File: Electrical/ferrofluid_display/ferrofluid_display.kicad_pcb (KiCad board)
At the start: 2 copper layers, 627 parts, among them J1001 Screw_Terminal_01x06, U100001 DRV8872DDAR, U10001 DRV8872DDAR, U1001 74HC595, U101001 DRV8872DDAR, U102001 DRV8872DDAR, U103001 DRV8872DDAR, U105001 DRV8872DDAR, U106001 DRV8872DDAR, U107001 DRV8872DDAR, U108001 DRV8872DDAR, U109001 DRV8872DDAR, U110001 DRV8872DDAR, U11001 DRV8872DDAR, U111001 DRV8872DDAR, U112001 DRV8872DDAR, U113001 DRV8872DDAR, U114001 DRV8872DDAR, U12001 DRV8872DDAR, U13001 DRV8872DDAR, U14001 DRV8872DDAR, U15001 DRV8872DDAR, U17001 DRV8872DDAR, U18001 DRV8872DDAR, U19001 DRV8872DDAR, U20001 DRV8872DDAR, U2002 74HC595, U2003 74HC595, U2004 74HC595, U2005 74HC595, U2006 74HC595, U2007 74HC595, U2008 74HC595, U2009 74HC595, U21001 DRV8872DDAR, U22001 DRV8872DDAR, U23001 DRV8872DDAR, U24001 DRV8872DDAR, U25001 DRV8872DDAR, U26001 DRV8872DDAR, U28001 DRV8872DDAR, U29001 DRV8872DDAR, U30001 DRV8872DDAR, U3002 74HC595, U3003 74HC595, U3004 74HC595, U3005 74HC595, U3006 74HC595, U3007 74HC595, U3008 74HC595, U3009 74HC595, U31001 DRV8872DDAR, U32001 DRV8872DDAR, U33001 DRV8872DDAR, U34001 DRV8872DDAR, U35001 DRV8872DDAR, U36001 DRV8872DDAR, U37001 DRV8872DDAR, U39001 DRV8872DDAR, U40001 DRV8872DDAR, U4002 74HC595, U4003 74HC595, U4004 74HC595, U4005 74HC595, U4006 74HC595, U4007 74HC595, U4008 74HC595, U4009 74HC595, U41001 DRV8872DDAR, U42001 DRV8872DDAR, U43001 DRV8872DDAR, U44001 DRV8872DDAR, U45001 DRV8872DDAR, U46001 DRV8872DDAR, U47001 DRV8872DDAR, U48001 DRV8872DDAR, U50001 DRV8872DDAR, U51001 DRV8872DDAR, U52001 DRV8872DDAR, U53001 DRV8872DDAR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

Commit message: Auto-layed out file
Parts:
- moved R26002 272.6 mm to (277.5, 0.03)
- moved U26001 272.5 mm to (279.5, 6.05)
- moved U112001 271.5 mm to (247.5, 118.0)
- moved L112001 271.1 mm to (253.2, 117.9), turned to 90 degrees
- moved R15002 270.9 mm to (277.5, -14.0)
- moved D26002 270.6 mm to (281.2, -0.10), turned to 180 degrees
- moved U103001 270.5 mm to (279.5, 104.0)
- moved L103001 270.0 mm to (285.2, 103.9), turned to 90 degrees
- moved U15001 268.9 mm to (279.5, -7.95)
- moved L26001 268.6 mm to (285.2, 5.87), turned to 90 degrees
- moved D15002 268.2 mm to (281.2, -14.1), turned to 180 degrees
- moved D112002 266.0 mm to (249.2, 111.9), turned to 180 degrees
- moved D103002 265.0 mm to (281.2, 97.9), turned to 180 degrees
- moved R112002 264.9 mm to (245.5, 112.0)
- moved R103002 264.1 mm to (277.5, 98.0)
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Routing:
- net GND: track 0.00 -> 340.6 mm, vias 0 -> 200
- net Net-(D68002-Pad1): track 0.00 -> 14.0 mm
- net Net-(D67002-Pad1): track 0.00 -> 14.0 mm
- net Net-(D66002-Pad1): track 0.00 -> 14.0 mm
- net Net-(D65002-Pad1): track 0.00 -> 14.0 mm
- net Net-(D64002-Pad1): track 0.00 -> 14.0 mm
- net Net-(D63002-Pad1): track 0.00 -> 14.0 mm
- net Net-(D62002-Pad1): track 0.00 -> 14.0 mm
- net Net-(D61002-Pad1): track 0.00 -> 14.0 mm
- net Net-(D57002-Pad1): track 0.00 -> 14.0 mm
- net Net-(D56002-Pad1): track 0.00 -> 14.0 mm
- net Net-(D55002-Pad1): track 0.00 -> 14.0 mm
- net Net-(D54002-Pad1): track 0.00 -> 14.0 mm
- net Net-(D53002-Pad1): track 0.00 -> 14.0 mm
- net Net-(D52002-Pad1): track 0.00 -> 14.0 mm
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
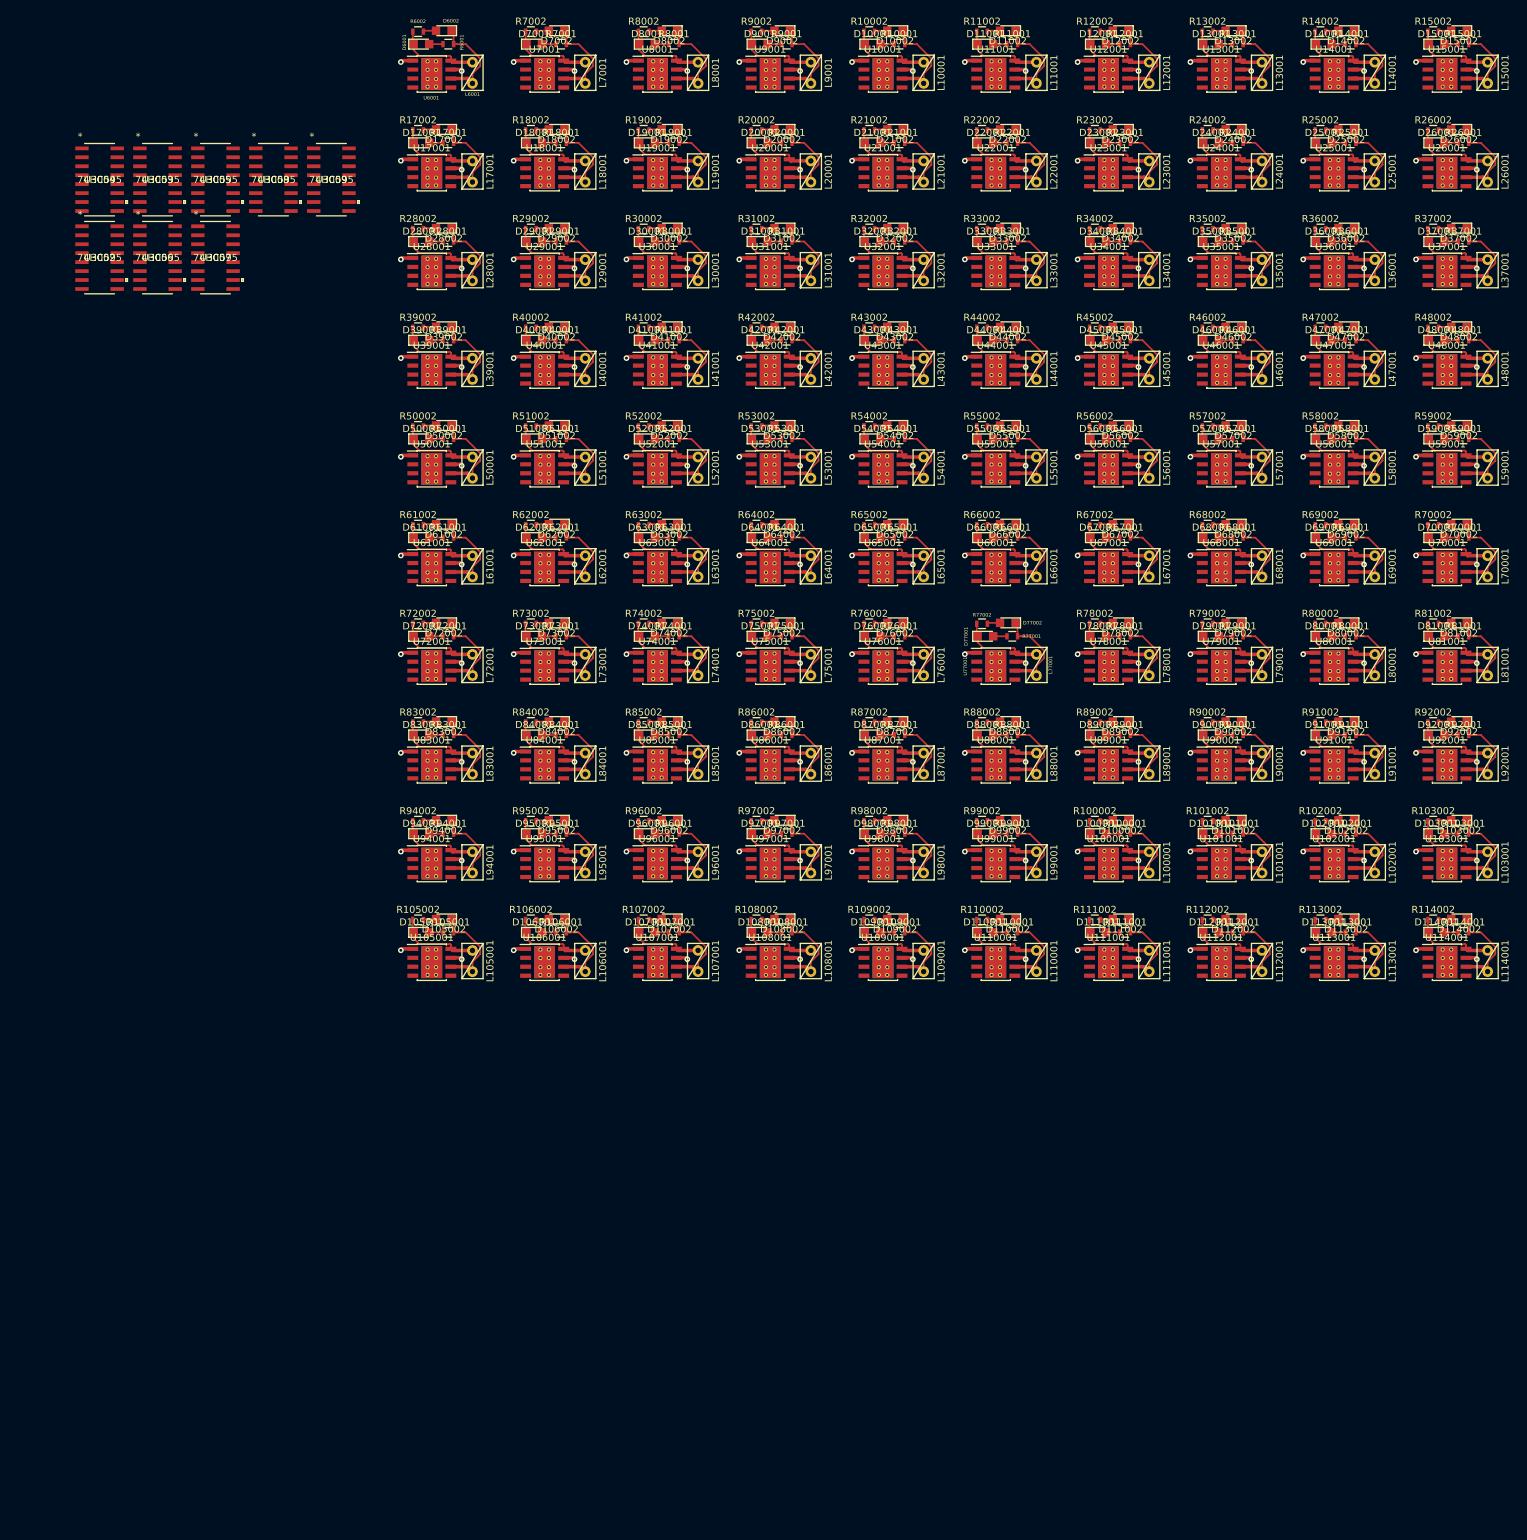
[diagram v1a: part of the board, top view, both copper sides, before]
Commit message: Added layers and 5V via
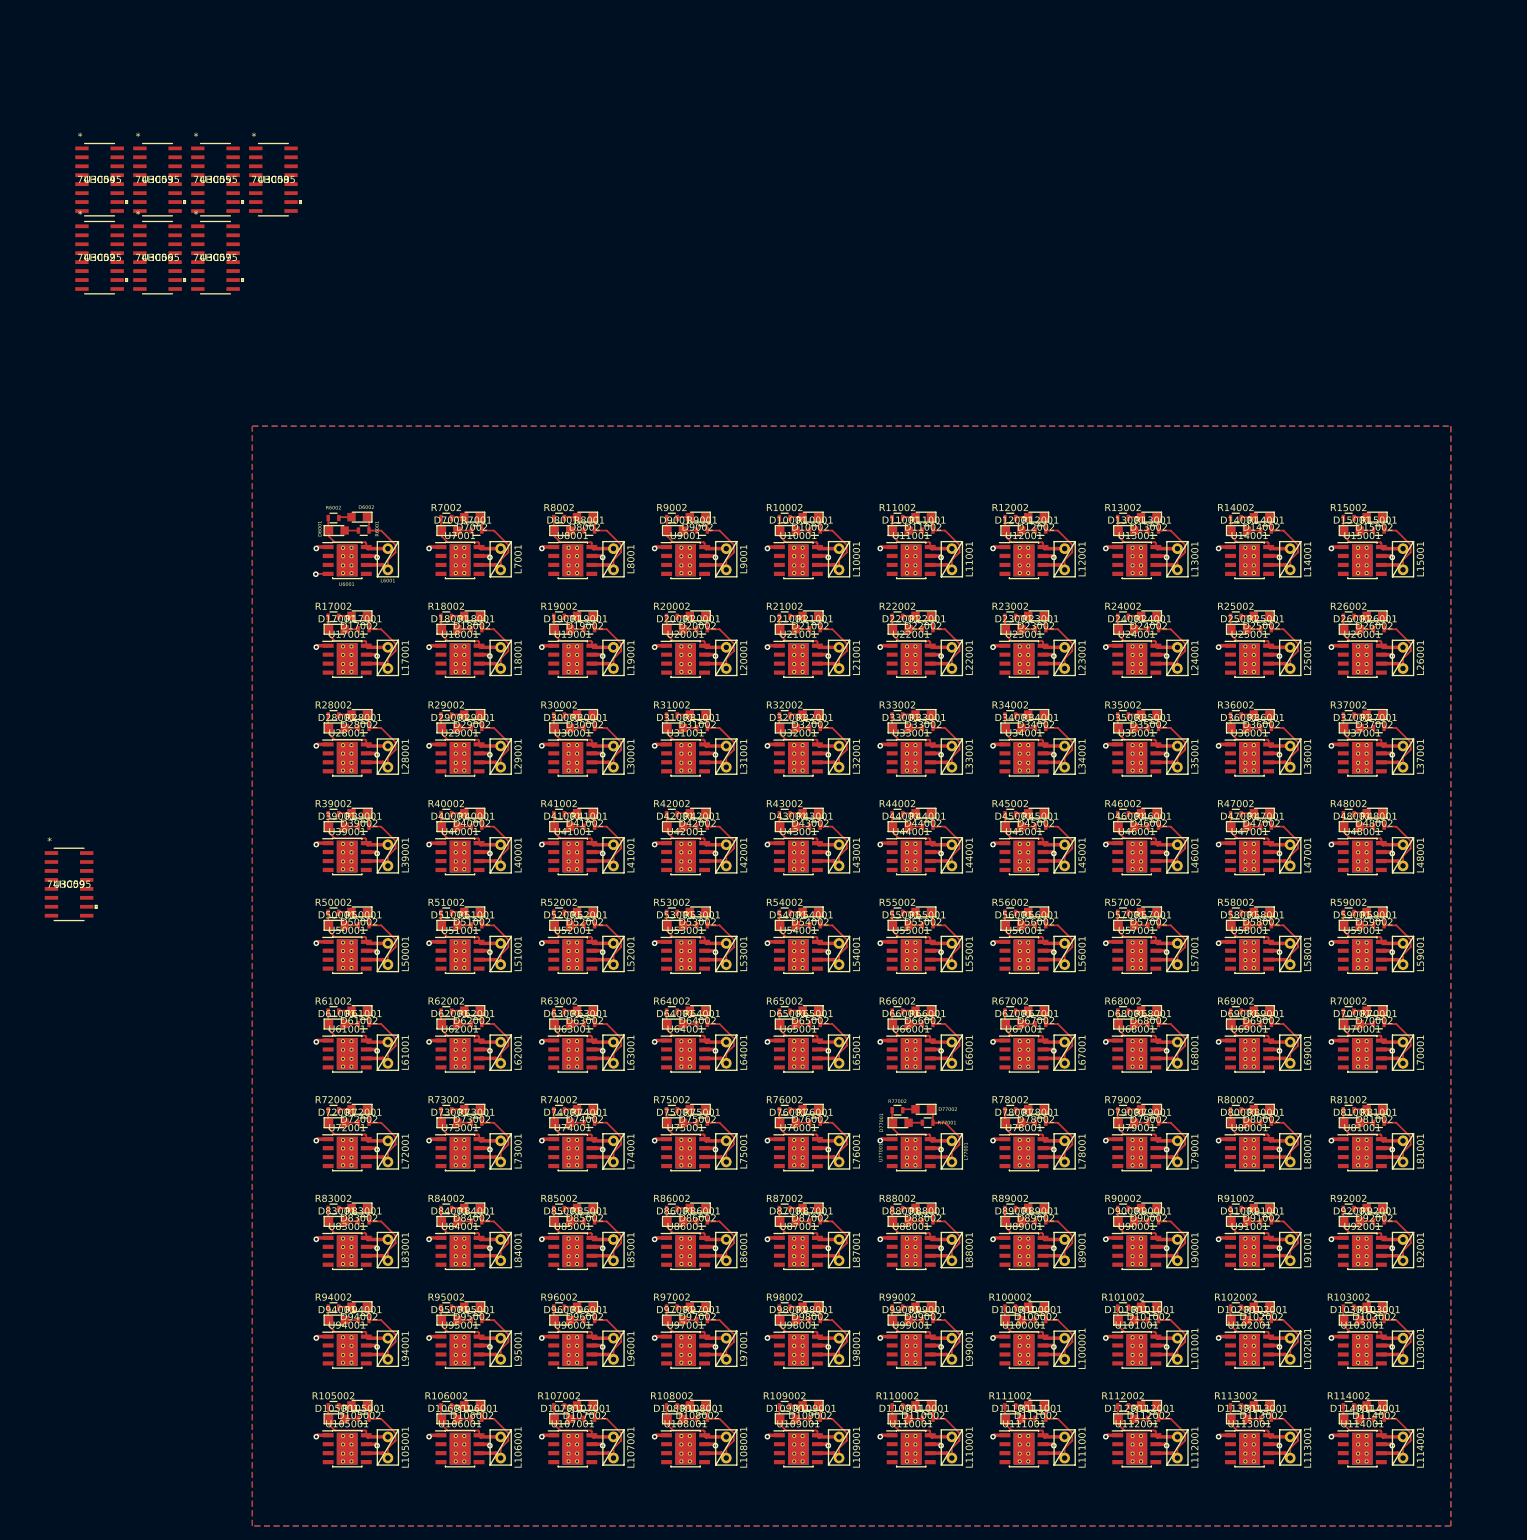
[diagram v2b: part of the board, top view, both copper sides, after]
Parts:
- moved U3009 106.7 mm to (84.0, 107.0)
- moved L100001 70.0 mm to (225.2, 172.9)
- moved L101001 70.0 mm to (241.2, 172.9)
- moved L102001 70.0 mm to (257.2, 172.9)
- moved L103001 70.0 mm to (273.2, 172.9)
- moved L105001 70.0 mm to (129.2, 186.9)
- moved L106001 70.0 mm to (145.2, 186.9)
- moved L107001 70.0 mm to (161.2, 186.9)
- moved L108001 70.0 mm to (177.2, 186.9)
- moved L109001 70.0 mm to (193.2, 186.9)
- moved L110001 70.0 mm to (209.2, 186.9)
- moved L111001 70.0 mm to (225.2, 186.9)
- moved L112001 70.0 mm to (241.2, 186.9)
- moved L113001 70.0 mm to (257.2, 186.9)
- moved L114001 70.0 mm to (273.2, 186.9)
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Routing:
- net +5V: track 0.00 -> 1.78 mm, vias 0 -> 1
- added copper zone on F.Cu, net +12V
- added copper zone on In1.Cu, net +5V
- added copper zone on B.Cu, net GND
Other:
- copper layers 2 -> 4

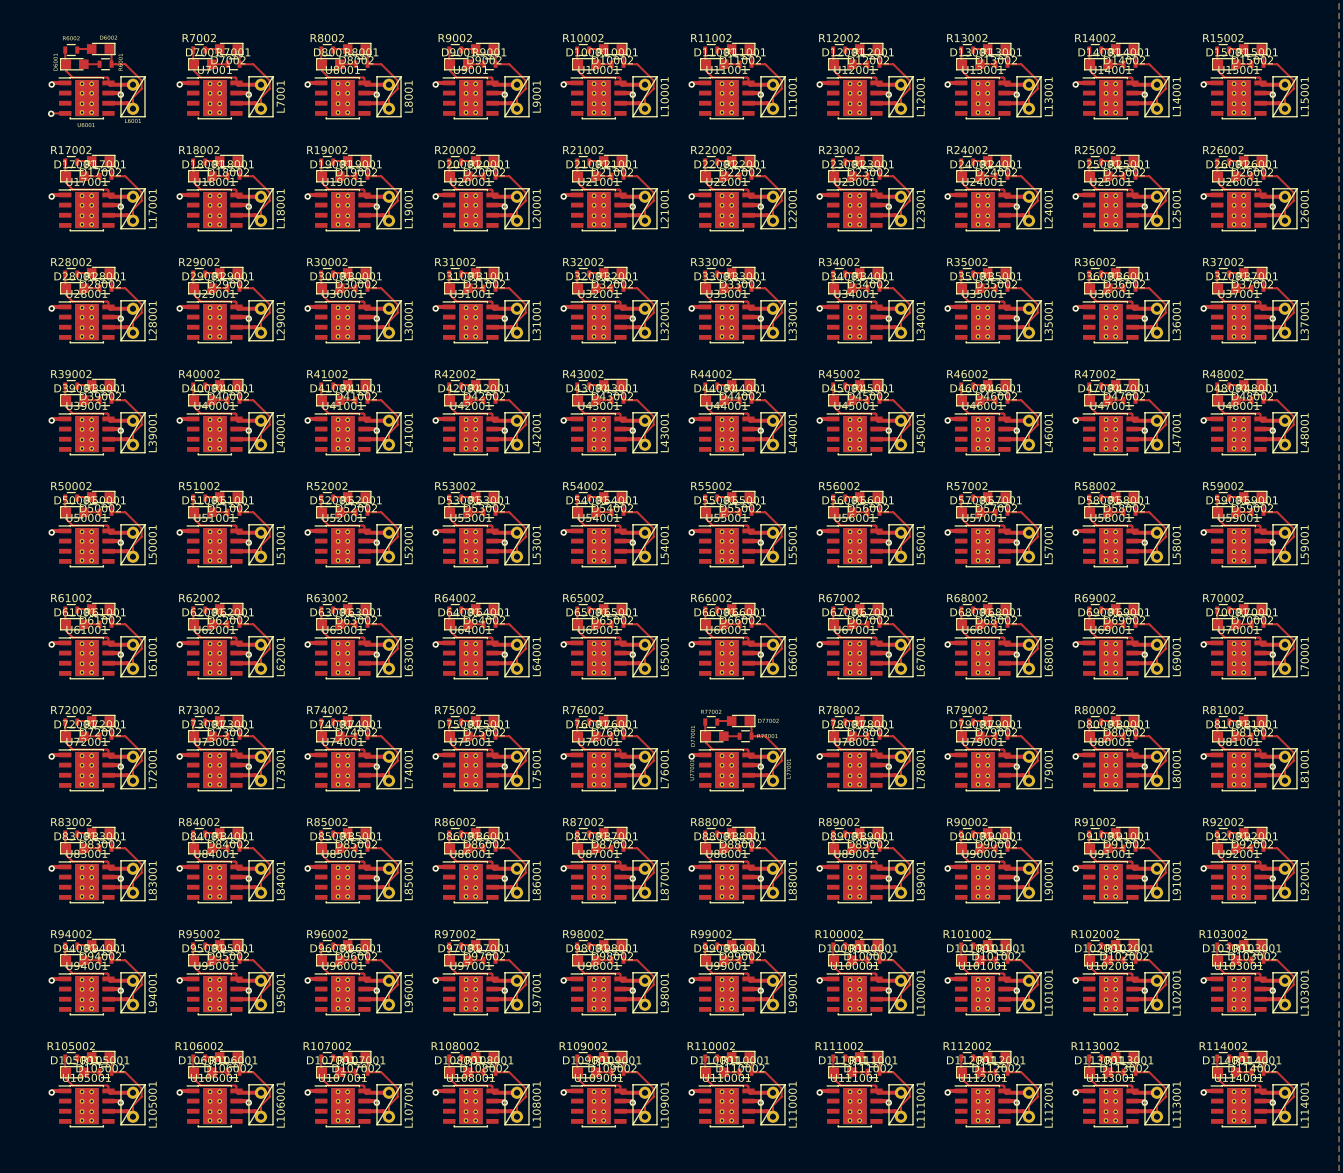
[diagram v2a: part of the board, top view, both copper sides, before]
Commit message: Propegated 5V changes
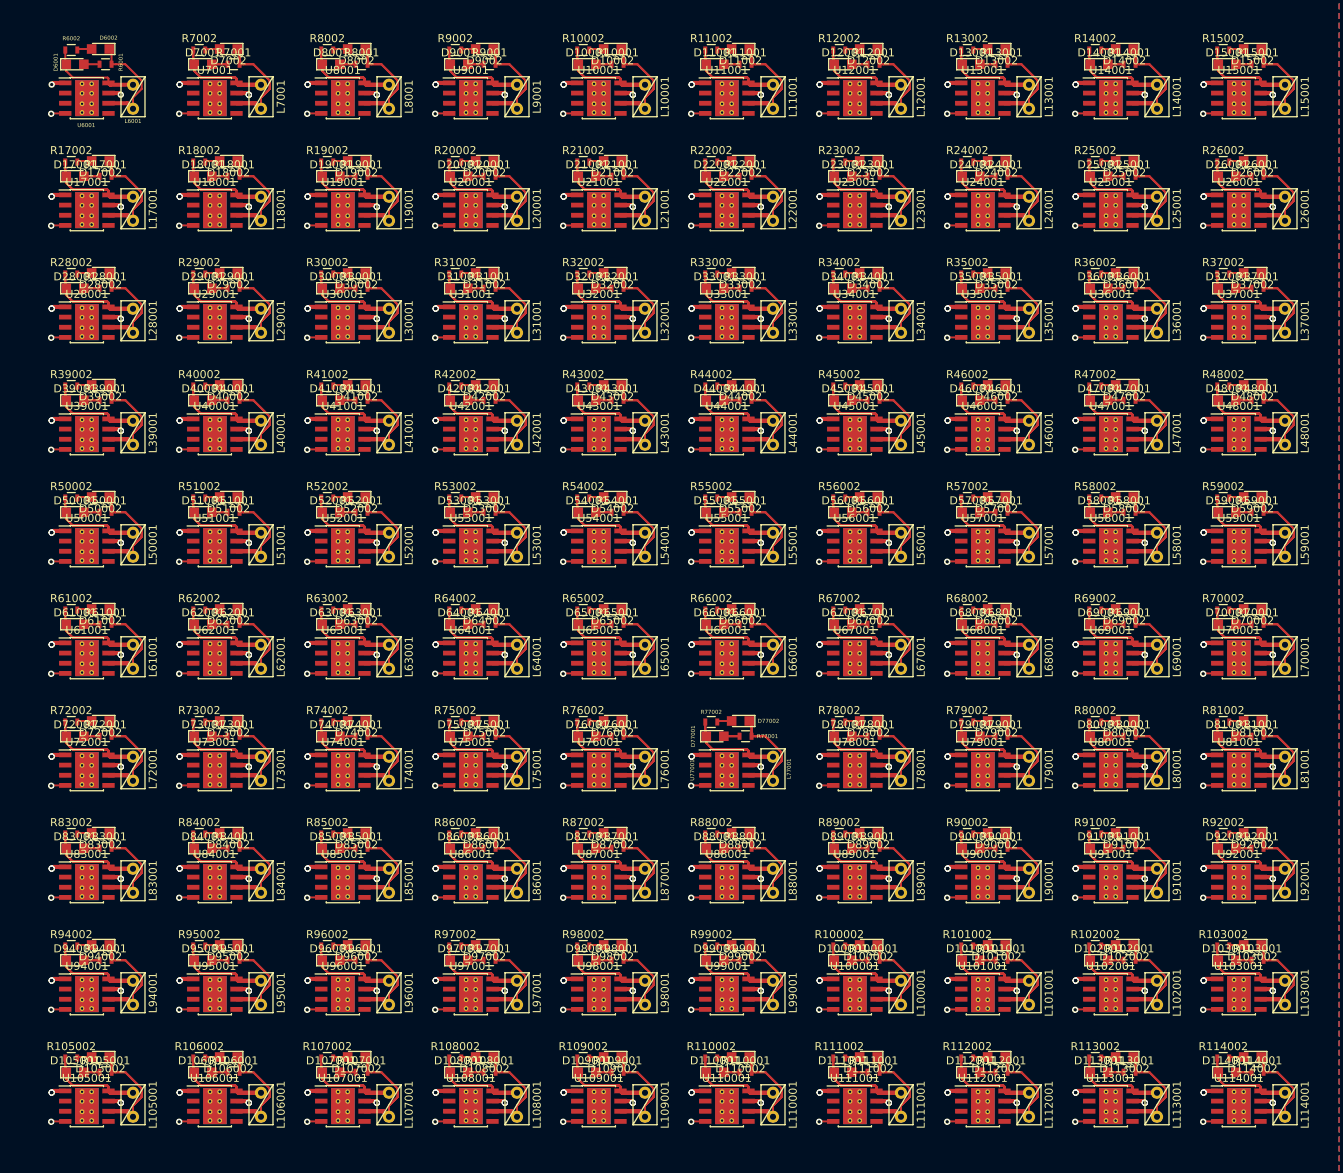
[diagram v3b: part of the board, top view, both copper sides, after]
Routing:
- net GND: track 340.6 -> 677.8 mm, vias 200 -> 398
- net +5V: track 1.78 -> 177.7 mm, vias 1 -> 100
- net Net-(D99002-Pad1): track 14.0 -> 27.9 mm
- net Net-(D98002-Pad1): track 14.0 -> 27.9 mm
- net Net-(D97002-Pad1): track 14.0 -> 27.9 mm
- net Net-(D96002-Pad1): track 14.0 -> 27.9 mm
- net Net-(D95002-Pad1): track 14.0 -> 27.9 mm
- net Net-(D90002-Pad1): track 14.0 -> 27.9 mm
- net Net-(D89002-Pad1): track 14.0 -> 27.9 mm
- net Net-(D88002-Pad1): track 14.0 -> 27.9 mm
- net Net-(D87002-Pad1): track 14.0 -> 27.9 mm
- net Net-(D86002-Pad1): track 14.0 -> 27.9 mm
- net Net-(D85002-Pad1): track 14.0 -> 27.9 mm
- net Net-(D84002-Pad1): track 14.0 -> 27.9 mm
- net Net-(D79002-Pad1): track 14.0 -> 27.9 mm
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
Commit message: Routed most of bord
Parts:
- moved U1001 327.0 mm to (281.0, 185.0)
- moved U4005 295.3 mm to (281.0, 172.0)
- moved U2009 286.0 mm to (281.0, 75.0)
- moved U4002 278.3 mm to (281.0, 115.0)
- moved U2004 269.8 mm to (281.0, 61.0)
- moved U4007 256.5 mm to (281.0, 129.0)
- moved U2006 236.2 mm to (205.2, 196.0), turned to 270 degrees
- moved U3003 230.3 mm to (281.0, 145.0)
- moved U3008 226.5 mm to (281.0, 159.0)
- moved J1001 226.3 mm to (248.0, 31.0), turned to 180 degrees
- moved U4004 214.9 mm to (188.6, 196.0), turned to 270 degrees
- moved U3005 200.2 mm to (281.0, 102.0)
- moved U3006 197.6 mm to (281.0, 89.0)
- moved U2008 185.2 mm to (188.0, 48.0), turned to 90 degrees
- moved U2003 184.8 mm to (204.0, 48.0), turned to 90 degrees
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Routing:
- net GND: track 677.8 -> 395.2 mm, vias 398 -> 234
- net /O_61: track 0.00 -> 245.7 mm, vias 0 -> 5
- net /O_21: track 0.00 -> 244.9 mm, vias 0 -> 5
- net /O_22: track 0.00 -> 242.2 mm, vias 0 -> 5
- net /O_101: track 0.00 -> 231.8 mm, vias 0 -> 3
- net /O_62: track 0.00 -> 231.4 mm, vias 0 -> 5
- net /O_102: track 0.00 -> 230.7 mm, vias 0 -> 3
- net /O_180: track 0.00 -> 224.6 mm, vias 0 -> 4
- net /O_103: track 0.00 -> 223.9 mm, vias 0 -> 4
- net /O_179: track 0.00 -> 223.3 mm, vias 0 -> 3
- net /O_23: track 0.00 -> 219.2 mm, vias 0 -> 3
- net /O_104: track 0.00 -> 218.4 mm, vias 0 -> 4
- net /O_177: track 0.00 -> 216.2 mm, vias 0 -> 4
- net /O_63: track 0.00 -> 215.0 mm, vias 0 -> 3
- net /O_24: track 0.00 -> 214.0 mm, vias 0 -> 3
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- added copper zone on In2.Cu, net +5V
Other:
- board outline added: 181 x 183 mm
